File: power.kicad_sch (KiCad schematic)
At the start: 48 parts, among them Q1 PMOS, Q2 NMOS, U1 BQ24074RGT, U2 TPS7A20xxxDQN, U3 LM27762, U4 TPS62840DLCR

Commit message: pcb / inital work
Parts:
- added R40: 10k, Resistor_SMD:R_0603_1608Metric, symbol PCM_Elektuur:R
- C10, C13, C14, C15, C16, C17, C18, C21, C3, C9: footprint Capacitor_THT:C_Disc_D3.0mm_W2.0mm_P2.50mm -> Capacitor_SMD:C_0603_1608Metric
- C2: footprint Capacitor_THT:C_Disc_D3.0mm_W2.0mm_P2.50mm -> Capacitor_SMD:C_0805_2012Metric
- FB1: footprint (none) -> PCM_Ferrite_SMD_AKL:Ferrite_0805_2012Metric
- FB3, FB4: footprint (none) -> PCM_Ferrite_SMD_AKL:Ferrite_0603_1608Metric
- JP3, JP4: footprint (none) -> PCM_Jumper_AKL:Jumper_P2.54mm_D0.7mm
- L1: footprint (none) -> Inductor_SMD:L_1008_2520Metric
- Q1, Q2: footprint (none) -> Package_TO_SOT_SMD:SOT-23
- R1, R10, R13, R18, R19, R2, R20, R22, R23, R24, R34, R35, R4, R8, R9: footprint (none) -> Resistor_SMD:R_0603_1608Metric
- R3: value R -> 1.2k; footprint (none) -> Resistor_SMD:R_0603_1608Metric
- TH1: value Thermistor -> NTC 10k; footprint (none) -> Resistor_SMD:R_0603_1608Metric
- U4: footprint TPS62840DLCR:SON50P200X150X100-8N -> uwu:SON50P200X150X100-8N
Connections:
- net BAT_TEMP: now also R40.2 (-)
- net V3.3_SYS: no longer U2.3 (EN), U3.12 (EN+), U3.8 (EN-)
- net VSYS: now also R40.1 (+)
- new net AUDIO_EN: U2.3 (EN), U3.12 (EN+), U3.8 (EN-)
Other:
- moved on the sheet: TH1

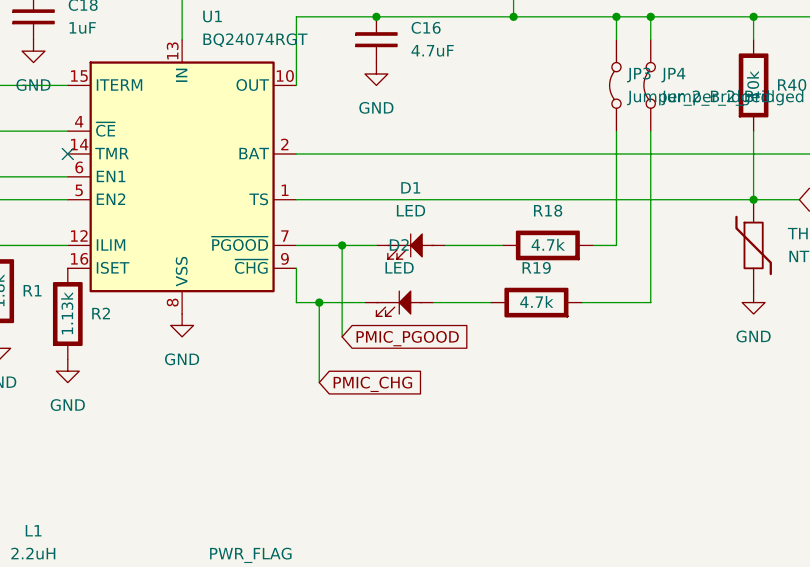
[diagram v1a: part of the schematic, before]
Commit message: ICs placed
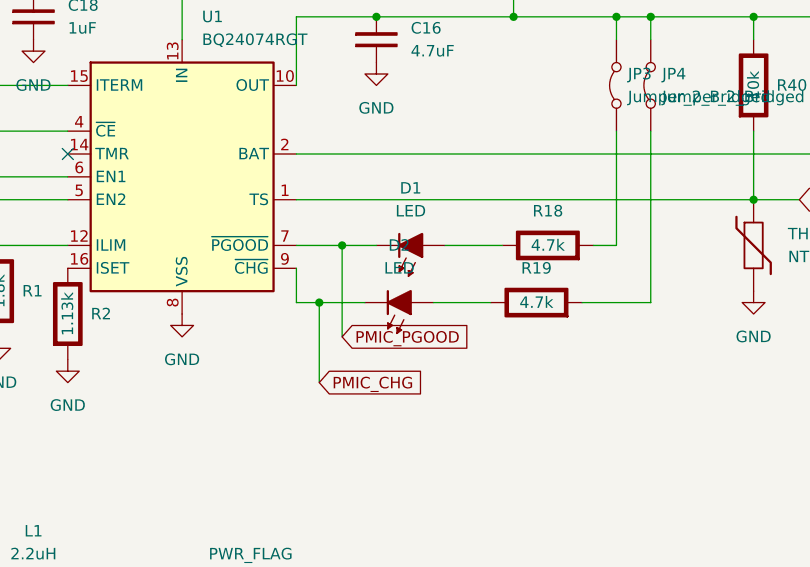
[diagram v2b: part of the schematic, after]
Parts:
- D1, D2: footprint LED_THT:LED_D5.0mm -> PCM_LED_SMD_AKL:LED_PLCC-2_2216; symbol PCM_SL_Devices:LED -> PCM_LED_AKL:LED_PLCC2_2.2x1.6
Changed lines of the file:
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@@
 	)
 	(symbol
-		(lib_id "PCM_SL_Devices:LED")
+		(lib_id "PCM_LED_AKL:LED_PLCC2_2.2x1.6")
 		(at 147.32 60.96 180)
 		(unit 1)
@@
 			)
 		)
-		(property "Footprint" "LED_THT:LED_D5.0mm"
-			(at 148.336 58.166 0)
-			(effects
-				(font
-					(size 1.27 1.27)
-				)
-				(hide yes)
-			)
-		)
-		(property "Datasheet" ""
-			(at 148.59 60.96 0)
-			(effects
-				(font
-					(size 1.27 1.27)
-				)
-				(hide yes)
-			)
-		)
-		(property "Description" "Common 5mm diameter LED"
+		(property "Footprint" "PCM_LED_SMD_AKL:LED_PLCC-2_2216"
+			(at 147.32 60.96 0)
+			(effects
+				(font
+					(size 1.27 1.27)
+				)
+				(hide yes)
+			)
+		)
+		(property "Datasheet" "~"
+			(at 147.32 60.96 0)
+			(effects
+				(font
+					(size 1.27 1.27)
+				)
+				(hide yes)
+			)
+		)
+		(property "Description" "SMD LED, PLCC2 2.2mm length, 1.6mm width, Alternate KiCad Library"
 			(at 147.32 60.96 0)
 			(effects
@@
 	)
 	(symbol
-		(lib_id "PCM_SL_Devices:LED")
+		(lib_id "PCM_LED_AKL:LED_PLCC2_2.2x1.6")
 		(at 148.59 54.61 180)
 		(unit 1)
@@
 			)
 		)
-		(property "Footprint" "LED_THT:LED_D5.0mm"
-			(at 149.606 51.816 0)
-			(effects
-				(font
-					(size 1.27 1.27)
-				)
-				(hide yes)
-			)
-		)
-		(property "Datasheet" ""
-			(at 149.86 54.61 0)
-			(effects
-				(font
-					(size 1.27 1.27)
-				)
-				(hide yes)
-			)
-		)
-		(property "Description" "Common 5mm diameter LED"
+		(property "Footprint" "PCM_LED_SMD_AKL:LED_PLCC-2_2216"
 			(at 148.59 54.61 0)
 			(effects
+				(font
+					(size 1.27 1.27)
+				)
+				(hide yes)
+			)
+		)
+		(property "Datasheet" "~"
+			(at 148.59 54.61 0)
+			(effects
+				(font
+					(size 1.27 1.27)
+				)
+				(hide yes)
+			)
+		)
+		(property "Description" "SMD LED, PLCC2 2.2mm length, 1.6mm width, Alternate KiCad Library"
+			(at 148.59 54.61 0)
+			(effects

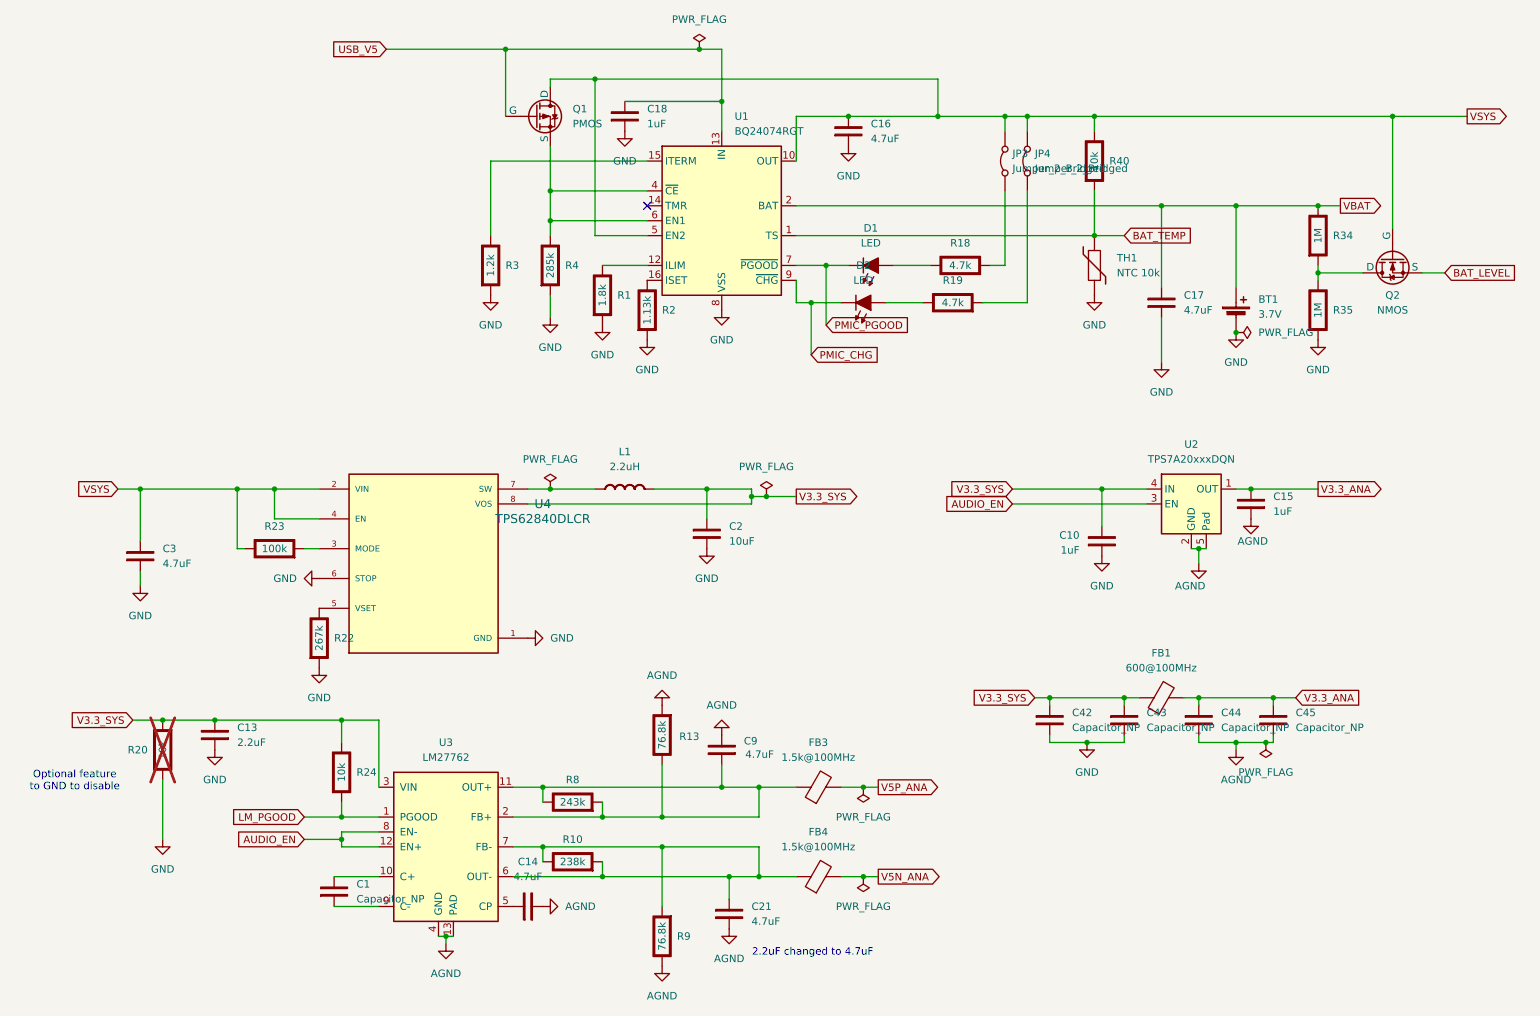
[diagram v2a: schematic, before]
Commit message: all pcb elements positioned + minor schematics changes
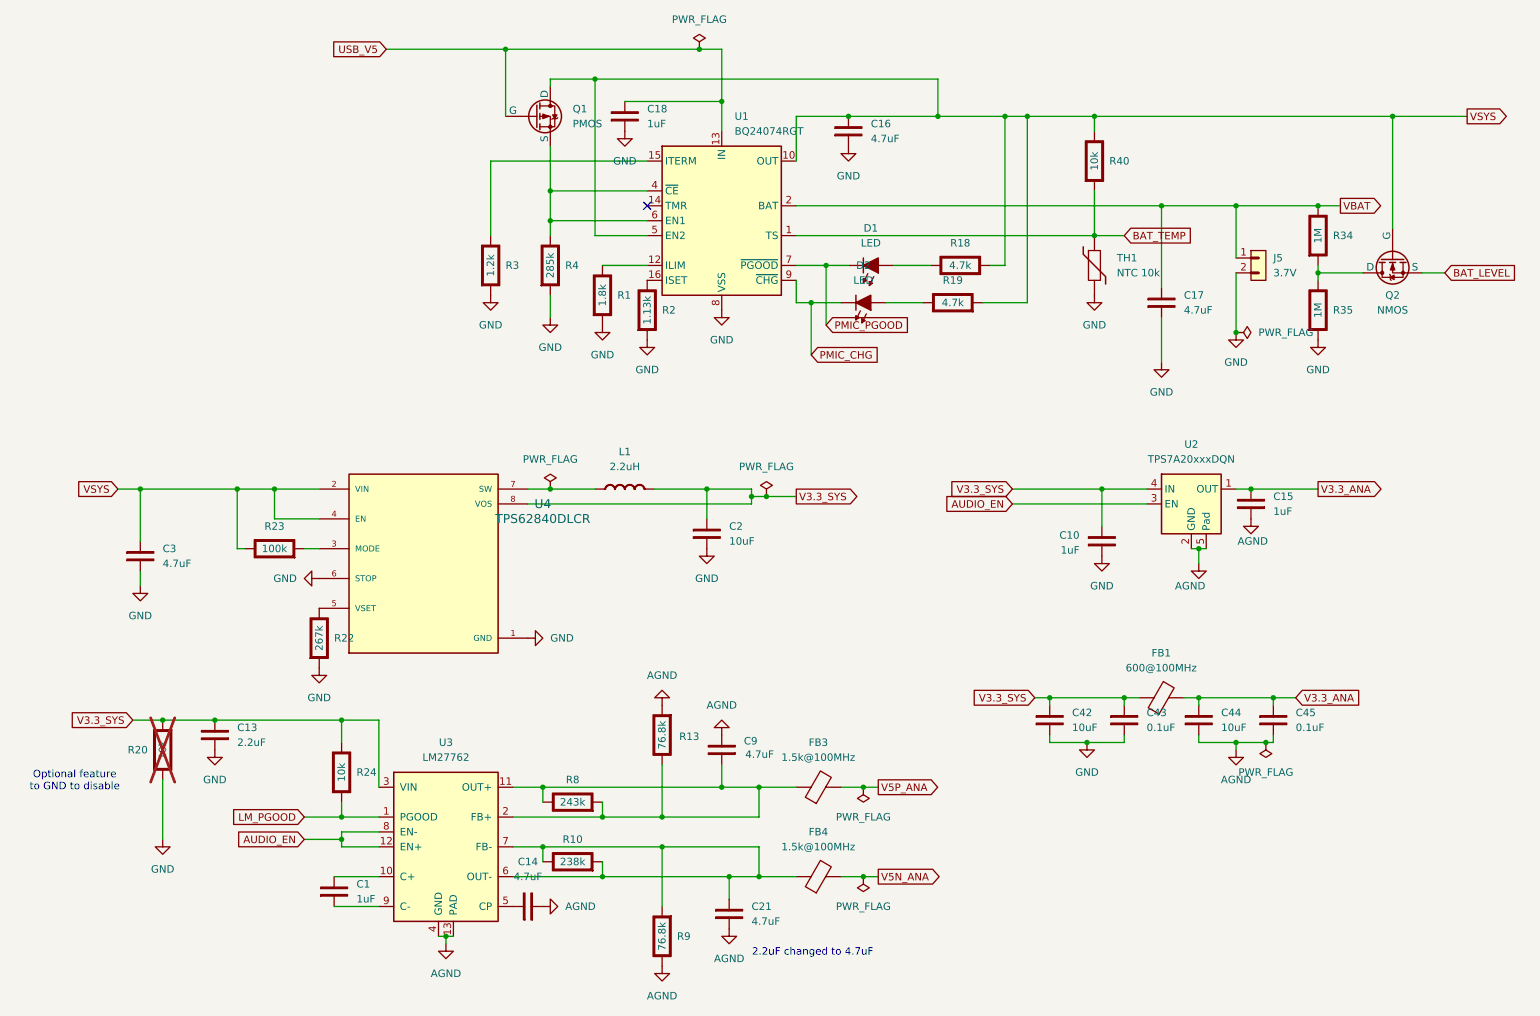
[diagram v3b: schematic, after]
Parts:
- removed BT1: 3.7V, symbol Device:Battery_Cell
- removed JP3, JP4: Jumper_2_Bridged, PCM_Jumper_AKL:Jumper_P2.54mm_D0.7mm, symbol Jumper:Jumper_2_Bridged
- added J5: 3.7V, uwu:CONN_B2B-ZR-SM4-TF_JST, symbol PCM_SL_Pin_Headers:PINHD_1x2_Male
- C1: value Capacitor_NP -> 1uF; footprint Capacitor_THT:C_Disc_D3.0mm_W2.0mm_P2.50mm -> Capacitor_SMD:C_0603_1608Metric
- C42, C44: value Capacitor_NP -> 10uF; footprint Capacitor_THT:C_Disc_D3.0mm_W2.0mm_P2.50mm -> Capacitor_Tantalum_SMD:CP_EIA-3528-21_Kemet-B
- C43, C45: value Capacitor_NP -> 0.1uF; footprint Capacitor_THT:C_Disc_D3.0mm_W2.0mm_P2.50mm -> Capacitor_SMD:C_0603_1608Metric
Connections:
- net GND: now also J5.2
- net VBAT: now also J5.1
- net VSYS: now also R18.2 (-), R19.2 (-)

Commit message: non ci sono parole adatte a descrivere la mia sofferenza
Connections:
- net GND is gone; now on net AGND: C10.1, C13.2, C16.1, C17.1, C18.1, C2.1, C3.1, C42.1, C43.1, J5.2, R1.2 (-), R2.2 (-), R20.1 (+), R22.2 (-), R3.2 (-), R35.2 (-), R4.2 (-), TH1.2, U1.17 (VSS), U1.8 (VSS), U4.1 (GND), U4.6 (STOP)
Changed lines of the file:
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@@
 	(wire
 		(pts
+			(xy 142.24 119.38) (xy 147.32 119.38)
+		)
+		(stroke
+			(width 0)
+			(type default)
+		)
+	)
+	(wire
+		(pts
 			(xy 179.07 128.27) (xy 191.77 128.27)
 		)
@@
 	(symbol
 		(lib_id "power:GND")
+		(at 147.32 119.38 0)
+		(unit 1)
+		(exclude_from_sim no)
+		(in_bom yes)
+		(on_board yes)
+		(dnp no)
+		(fields_autoplaced yes)
+		(property "Reference" "#PWR088"
+			(at 147.32 125.73 0)
+			(effects
+				(font
+					(size 1.27 1.27)
+				)
+				(hide yes)
+			)
+		)
+		(property "Value" "AGND"
+			(at 147.32 124.46 0)
+			(effects
+				(font
+					(size 1.27 1.27)
+				)
+			)
+		)
+		(property "Footprint" ""
+			(at 147.32 119.38 0)
+			(effects
+				(font
+					(size 1.27 1.27)
+				)
+				(hide yes)
+			)
+		)
+		(property "Datasheet" ""
+			(at 147.32 119.38 0)
+			(effects
+				(font
+					(size 1.27 1.27)
+				)
+				(hide yes)
+			)
+		)
+		(property "Description" "Power symbol creates a global label with name \"GND\" , ground"
+			(at 147.32 119.38 0)
+			(effects
+				(font
+					(size 1.27 1.27)
+				)
+				(hide yes)
+			)
+		)
+		(pin "1"
+		)
+		(instances
+			(project "owo"
+				(path "/bf8ac4c6-d1c7-49a9-8a5e-5cf20f43f3d7/6b0b92cb-7d95-445a-aef9-e7e37f35535b"
+					(reference "#PWR088")
+					(unit 1)
+				)
+			)
+		)
+	)
+	(symbol
+		(lib_id "power:GND")
 		(at 124.46 167.64 0)
 		(unit 1)
@@
 					(unit 1)
 				)
+			)
+		)
+	)
+	(symbol
+		(lib_id "power:GND")
+		(at 142.24 119.38 0)
+		(unit 1)
+		(exclude_from_sim no)
+		(in_bom yes)
+		(on_board yes)
+		(dnp no)
+		(fields_autoplaced yes)
+		(property "Reference" "#PWR087"
+			(at 142.24 125.73 0)
+			(effects
+				(font
+					(size 1.27 1.27)
+				)
+				(hide yes)
+			)
+		)
+		(property "Value" "GND"
+			(at 142.24 124.46 0)
+			(effects
+				(font
+					(size 1.27 1.27)
+				)
+			)
+		)
+		(property "Footprint" ""
+			(at 142.24 119.38 0)
+			(effects
+				(font
+					(size 1.27 1.27)
+				)
+				(hide yes)
+			)
+		)
+		(property "Datasheet" ""
+			(at 142.24 119.38 0)
+			(effects
+				(font
+					(size 1.27 1.27)
+				)
+				(hide yes)
+			)
+		)
+		(property "Description" "Power symbol creates a global label with name \"GND\" , ground"
+			(at 142.24 119.38 0)
+			(effects
+				(font
+					(size 1.27 1.27)
+				)
+				(hide yes)
+			)
+		)
+		(pin "1"
+		)
+		(instances
+			(project "owo"
+				(path "/bf8ac4c6-d1c7-49a9-8a5e-5cf20f43f3d7/6b0b92cb-7d95-445a-aef9-e7e37f35535b"
+					(reference "#PWR087")
+					(unit 1)
+				)
